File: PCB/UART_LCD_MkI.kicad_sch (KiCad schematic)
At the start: 7 parts, among them U1 CH32V003

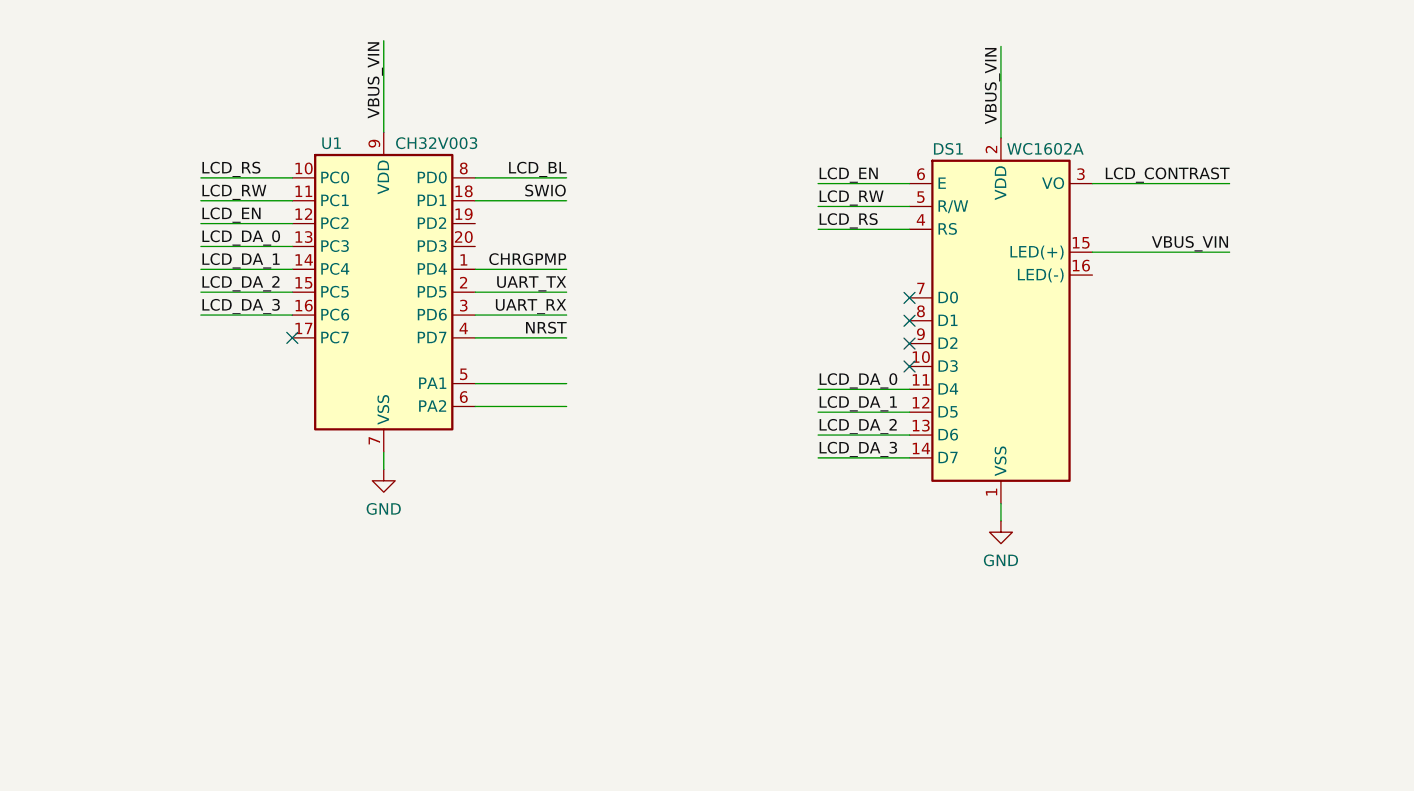
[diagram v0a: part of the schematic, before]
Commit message: Added BAUD Setting detection
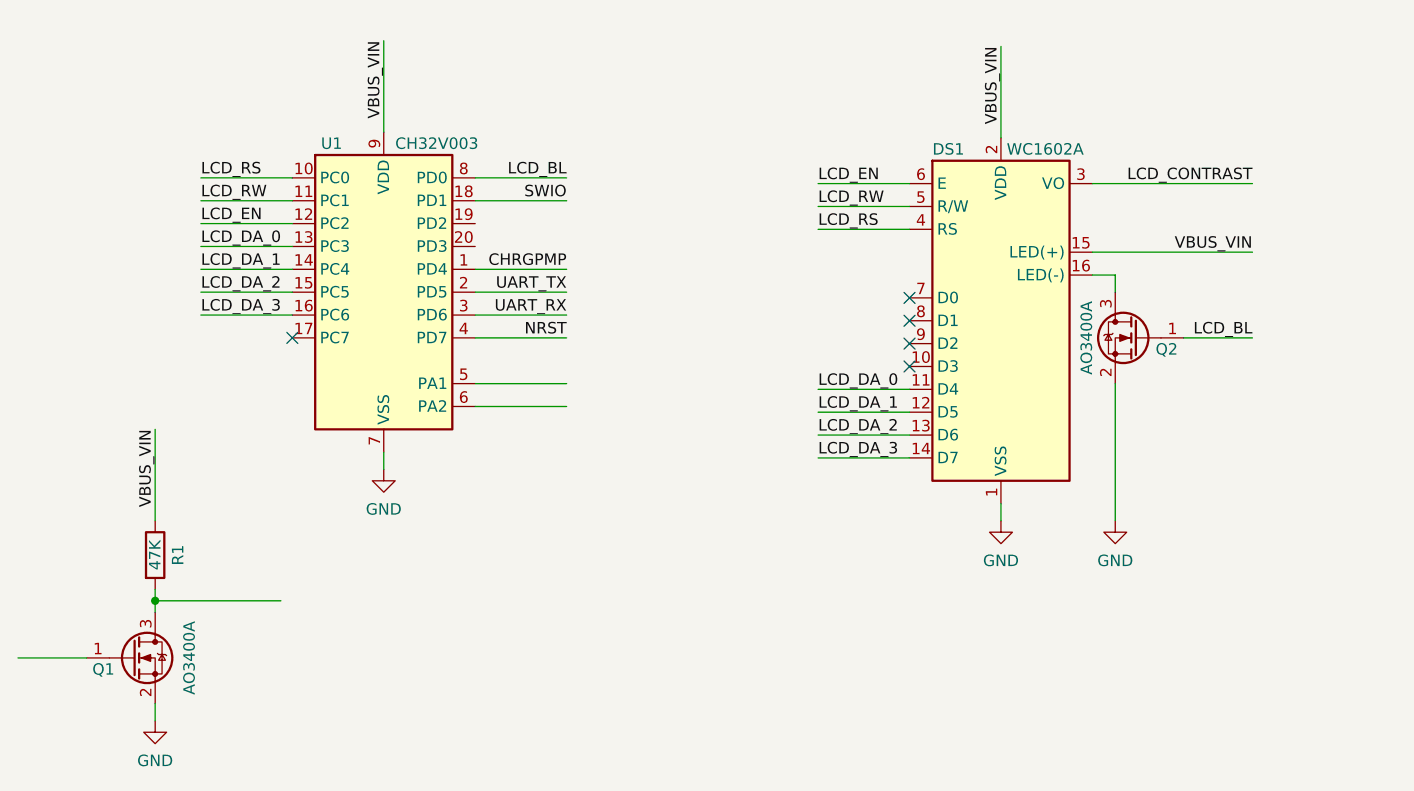
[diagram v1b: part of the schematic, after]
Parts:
- added Q1, Q2: AO3400A, Package_TO_SOT_SMD:SOT-23, symbol Transistor_FET:AO3400A
- added R1: 47K, symbol Device:R
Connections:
- net GND: now also Q1.2 (S), Q2.2 (S)
- net LCD_BL: now also Q2.1 (G)
- net VBUS_VIN: now also R1.1
- net at DS1.16 (LED(-)): now also Q2.3 (D)
- new net: Q1.3 (D), R1.2

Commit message: Added reverse protection to test & connectors
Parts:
- added C3: 1uF, Capacitor_SMD:C_0805_2012Metric, symbol Device:C_Small
- added J1: CONN_DATA, symbol Connector:Conn_01x03_Pin
- added J2: CONN_POWER, symbol Connector:Conn_01x02_Pin
- added Q3: AO3400A, Package_TO_SOT_SMD:SOT-23, symbol Transistor_FET:AO3400A
- added R2: 47K, symbol Device:R
- added TP1: VIN, symbol Connector:TestPoint
- added TP2: GND, symbol Connector:TestPoint
- added TP3: SWIO, symbol Connector:TestPoint
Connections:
- net GND: now also C3.1, J1.3 (Pin_3), J2.2 (Pin_2), Q3.3 (D), TP2.1
- net LCD_DA_0: now also U1.14 (PC4); no longer U1.13 (PC3)
- net LCD_DA_1: now also U1.15 (PC5); no longer U1.14 (PC4)
- net LCD_DA_2: now also U1.16 (PC6); no longer U1.15 (PC5)
- net LCD_DA_3: now also U1.17 (PC7); no longer U1.16 (PC6)
- net LCD_EN: now also U1.13 (PC3); no longer U1.12 (PC2)
- net LCD_RS: now also U1.11 (PC1); no longer U1.10 (PC0)
- net LCD_RW: now also U1.12 (PC2); no longer U1.11 (PC1)
- net SWIO: now also TP3.1
- net VBUS_VIN: now also C3.2, J2.1 (Pin_1), R2.1, TP1.1
- net BAUD_SEL0: now reaches U1.5 (PA1)
- net BAUD_SEL1: now reaches U1.6 (PA2)
- new net: Q3.1 (G), R2.2
- new net LOAD: Q3.2 (S)
- new net RS232_IN: J1.1 (Pin_1)
- new net UART_IN: J1.2 (Pin_2)
- no-connect marks 5 -> 7
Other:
- note added: "TODO"
- company: (none) -> ADBeta
- title: (none) -> UART_LCD

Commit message: Updated PCB
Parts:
- removed J1: CONN_DATA, symbol Connector:Conn_01x03_Pin
- removed Q1: AO3400A, Package_TO_SOT_SMD:SOT-23, symbol Transistor_FET:AO3400A
- removed R1: 47K, symbol Device:R
- added J1: CONN_DATA, Connector_PinHeader_2.54mm:PinHeader_1x02_P2.54mm_Vertical, symbol Connector:Conn_01x02_Pin
- J2: footprint (none) -> Connector_PinHeader_2.54mm:PinHeader_1x02_P2.54mm_Vertical
- R2: footprint (none) -> Resistor_SMD:R_0805_2012Metric
- RV1: footprint Resistor_SMD:R_0805_2012Metric -> Potentiometer_THT:Potentiometer_Bourns_3339P_Vertical
- TP1, TP2, TP3: footprint (none) -> TestPoint:TestPoint_Pad_D1.0mm
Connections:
- net GND: now also J1.2 (Pin_2)
- net UART_IN: now also J1.1 (Pin_1)
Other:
- moved on the sheet: C3, DS1, Q2, TP1, TP2, TP3, U1

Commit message: PCB Progress
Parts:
- added JP2: JMP_BL_GND, Jumper:SolderJumper-2_P1.3mm_Open_RoundedPad1.0x1.5mm, symbol Jumper:Jumper_2_Open
- added SW1: BAUD_SEL, Button_Switch_THT:SW_DIP_SPSTx02_Slide_9.78x7.26mm_W7.62mm_P2.54mm, symbol Switch:SW_DIP_x02
- DS1: footprint Display:WC1602A -> Connector_PinHeader_2.54mm:PinHeader_1x16_P2.54mm_Vertical
- R2: value 47K -> 4K7
- RV1: value 20K -> 100K
- renumbered J2 to J1, J1 to J2, Q3 to Q1
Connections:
- net LOAD is gone; now on net GND: Q1.2 (S)
- net UART_IN is gone; now on net UART_RX: J2.1 (Pin_1)
- net BAUD_SEL0: now also SW1.1
- net BAUD_SEL1: now also SW1.2
- net GND: now also JP2.1 (A); no longer J1.2 (Pin_2), Q1.3 (D)
- net VBUS_VIN: now also SW1.3, SW1.4
- net at DS1.16 (LED(-)), Q2.3 (D): now also JP2.2 (B)
- new net VBUS_GND: J1.2 (Pin_2), Q1.3 (D)
- no-connect marks 7 -> 9
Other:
- note added: "Input"
- note removed: "TODO"
- moved on the sheet: C3, DS1, J1, J2, Q1, Q2, R2, TP1, TP2, TP3, U1
